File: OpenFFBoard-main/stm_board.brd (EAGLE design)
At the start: 60 x 60 mm, 53 parts, among them J1 10118193-0001LF, SW1 TL3342F160QG/TR, SW2 TL3342F160QG/TR, U1 STM32(LQFP64), U2 NC7NZ17K8X-3-BUFFER, X1 8MHz

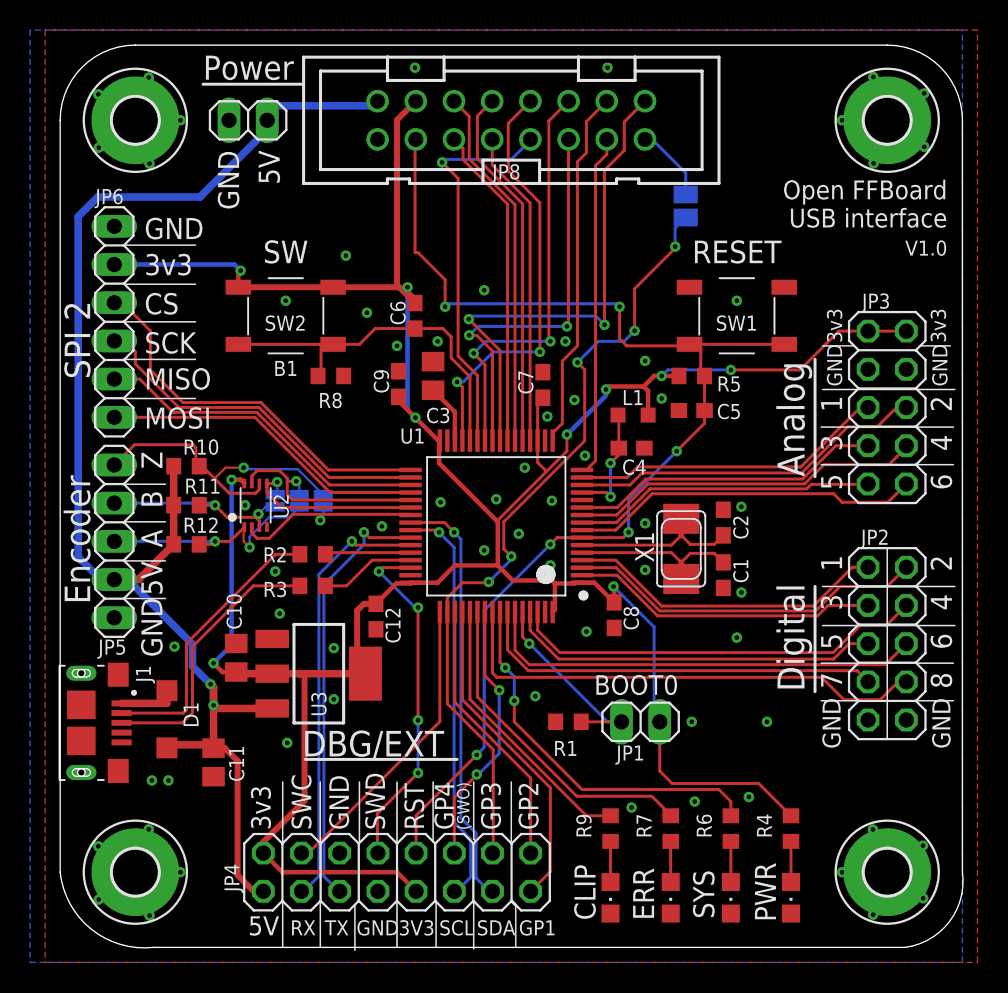
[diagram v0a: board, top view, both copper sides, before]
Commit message: Added 1.1.1 stm board
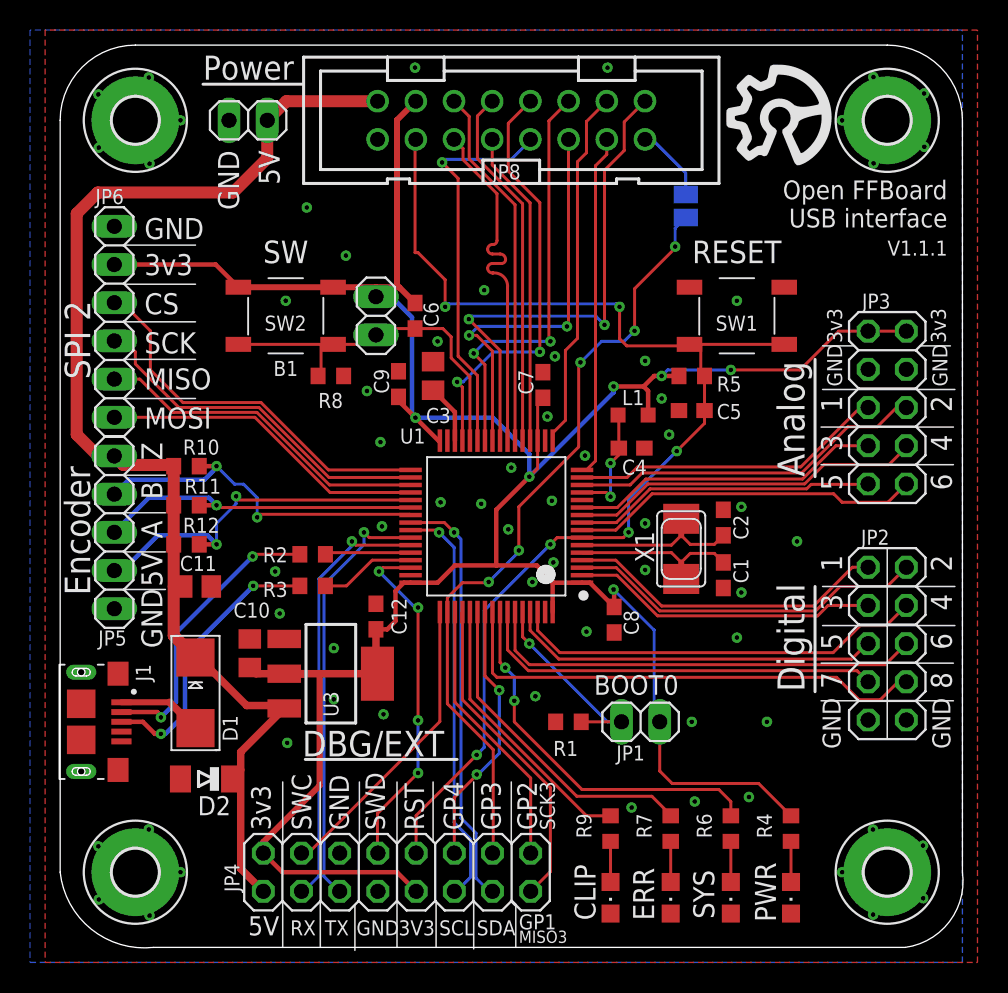
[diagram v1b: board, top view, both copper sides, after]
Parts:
- removed JP10, JP11: JUMPER-SMT_2_NO_NO-SILK, SparkFun-Jumpers:SMT-JUMPER_2_NO_NO-SILK
- removed U2: NC7NZ17K8X-3-BUFFER, Powermisc:VFSOP-8
- added D2: ZMM5V6, diode:MINIMELF
- D1: device diode:SOD123 -> adafruit:SMADIODE
- JP9: value JUMPER-SMT_2_NO_NO-SILK -> Btn; device SparkFun-Jumpers:SMT-JUMPER_2_NO_NO-SILK -> pinhead:1X02
- LED2: value yellow -> blue
- R4: value 330 -> 1k
- moved JP9 13.3 mm to (21.0, -18.0), flipped to the top, turned to 270 degrees
- moved C11 11.8 mm to (9.10, -36.0), turned to 0 degrees
- moved D1 2.59 mm to (9.00, -43.1), turned to 270 degrees
- moved C10 0.95 mm to (12.6, -40.4)
- moved U3 0.80 mm to (18.0, -41.8)
- moved JP5 0.60 mm to (3.60, -32.4)
- moved C8 0.30 mm to (36.8, -38.2)
- moved J1 0.07 mm to (1.40, -45.0)
- turned C12 to 90 degrees
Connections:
- removed net ENC_A_5V: JP5.3, JP9.1, R12.2, U2.P$1
- removed net ENC_B_5V: JP10.1, JP5.2, R11.2, U2.P$3
- removed net ENC_Z_5V: JP11.1, JP5.1, R10.2, U2.P$6
- net +3V3: now also JP9.1; no longer U2.P$8
- net +5V: now also D2.C, JP5.1; no longer JP5.4
- net BUTTON_A: now also JP9.2
- net ENC_A: now also JP5.4, R12.2; no longer JP9.2, U2.P$7
- net ENC_B: now also JP5.3, R11.2; no longer JP10.2, U2.P$5
- net ENC_Z: now also JP5.2, R10.2; no longer JP11.2, U2.P$2
- net GND: now also D2.A; no longer U2.P$4
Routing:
- net ENC_Z_5V: track 21.0 -> 0.00 mm, vias 1 -> 0
- net ENC_A_5V: track 16.5 -> 0.00 mm, vias 2 -> 0
- net ENC_B_5V: track 13.8 -> 0.00 mm, vias 2 -> 0
- net +3V3: track 200.0 -> 188.1 mm, vias 10 -> 6
- net +5V: track 94.6 -> 83.2 mm, vias 2 -> 0
- net ENC_Z: track 13.2 -> 24.0 mm, vias 1 -> 2
- net ENC_A: track 14.2 -> 24.7 mm, vias 1 -> 2
- net ENC_B: track 12.2 -> 22.1 mm
- net SPI1_MOSI: track 21.5 -> 23.7 mm
- net N$1: track 3.86 -> 5.64 mm
- net GPIO3: track 52.9 -> 52.0 mm
- net N$5: track 18.8 -> 19.3 mm, vias 0 -> 2
- net N$6: track 18.2 -> 18.6 mm, vias 0 -> 2
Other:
- board text added: "CS2 | CS3/PWM"
- board text added: "GP3 | EN"
- board text added: "MISO3"
- board text added: "SCK3"
- board text added: "SWO"
- board text added: "V1.1.1"
- board text added: "YR 2020"
- board text removed: "(SWO)"
- board text removed: "CS2 | CS3"
- board text removed: "ENC DIRECT"
- board text removed: "GPIO | EN"
- board text removed: "V1.0"
- board text removed: "YR 2019"
